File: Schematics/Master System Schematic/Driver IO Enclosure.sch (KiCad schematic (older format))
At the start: 0 parts

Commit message: New Relay Module Symbol/ Some Parts Added to Driver IO Container
(Note: Make sure to check that I didn't make some catastrophically horrible changes to everything by accident)
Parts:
- added A? (x2): Arduino_UNO_rev3, symbol NER:Arduino_UNO_rev3
- added K? (x2): G5Q-1, Relay_THT:Relay_SPDT_SANYOU_SRD_Series_Form_C, symbol Relay:G5Q-1
- added U?: CAN_Bus_Module, symbol NER:CAN_Bus_Module
- added U?: KY-019, symbol NER:KY-019
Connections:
- new net: A?.~ (~~D9), U?.~ (Serial_Clock)
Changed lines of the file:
@@
 EESchema Schematic File Version 4
-LIBS:Master System Schematic-cache
 EELAYER 30 0
 EELAYER END
@@
 Comment4 ""
 $EndDescr
+$Comp
+L Relay:G5Q-1 K?
+U 1 1 5F841D56
+P 2250 2800
+F 0 "K?" H 2680 2846 50  0000 L CNN
+F 1 "G5Q-1" H 2680 2755 50  0000 L CNN
+F 2 "Relay_THT:Relay_SPDT_SANYOU_SRD_Series_Form_C" H 2700 2750 50  0001 L CNN
+F 3 "https://www.omron.com/ecb/products/pdf/en-g5q.pdf" H 2250 2800 50  0001 L CNN
+	1    2250 2800
+	1    0    0    -1
+$EndComp
+$Comp
+L Relay:G5Q-1 K?
+U 1 1 5F84603E
+P 8500 1500
+F 0 "K?" H 8930 1546 50  0000 L CNN
+F 1 "G5Q-1" H 8930 1455 50  0000 L CNN
+F 2 "Relay_THT:Relay_SPDT_SANYOU_SRD_Series_Form_C" H 8950 1450 50  0001 L CNN
+F 3 "https://www.omron.com/ecb/products/pdf/en-g5q.pdf" H 8500 1500 50  0001 L CNN
+	1    8500 1500
+	-1   0    0    1
+$EndComp
+$Comp
+L NER:Arduino_UNO_rev3 A?
+U 1 1 5F8467E9
+P 2250 4000
+F 0 "A?" H 2250 4115 50  0000 C CNN
+F 1 "Arduino_UNO_rev3" H 2250 4024 50  0000 C CNN
+F 2 "" H 2250 4150 50  0001 C CNN
+F 3 "" H 2250 4150 50  0001 C CNN
+	1    2250 4000
+	1    0    0    -1
+$EndComp
+$Comp
+L NER:CAN_Bus_Module U?
+U 1 1 5F847676
+P 8650 2250
+F 0 "U?" H 8675 2365 50  0000 C CNN
+F 1 "CAN_Bus_Module" H 8675 2274 50  0000 C CNN
+F 2 "" H 8650 2250 50  0001 C CNN
+F 3 "" H 8650 2250 50  0001 C CNN
+	1    8650 2250
+	1    0    0    -1
+$EndComp
+$Comp
+L NER:Arduino_UNO_rev3 A?
+U 1 1 5F848DBE
+P 6800 2000
+F 0 "A?" H 6800 2115 50  0000 C CNN
+F 1 "Arduino_UNO_rev3" H 6800 2024 50  0000 C CNN
+F 2 "" H 6800 2150 50  0001 C CNN
+F 3 "" H 6800 2150 50  0001 C CNN
+	1    6800 2000
+	1    0    0    -1
+$EndComp
+Wire Wire Line
+	7400 2650 7800 2650
+Wire Wire Line
+	7800 2650 7800 2900
+Wire Wire Line
+	7800 2900 8100 2900
+$Comp
+L NER:KY-019 U?
+U 1 1 5F94DA0F
+P 3800 4300
+F 0 "U?" V 3375 4275 50  0000 C CNN
+F 1 "KY-019" V 3466 4275 50  0000 C CNN
+F 2 "" H 3750 4000 50  0001 C CNN
+F 3 "" H 3750 4000 50  0001 C CNN
+	1    3800 4300
+	0    1    1    0
+$EndComp
 $EndSCHEMATC

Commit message: Added Annotations
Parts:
- removed K? (x2): G5Q-1, Relay_THT:Relay_SPDT_SANYOU_SRD_Series_Form_C, symbol Relay:G5Q-1
- added U12: KY-019, symbol NER:KY-019
- gave numbers to parts that had none: 4
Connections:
- net at U11.~ (Serial_Clock): now also A3.~ (~~D9)
- net at A3.~ (~~D9): no longer U11.~ (Serial_Clock)
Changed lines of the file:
@@
 $EndDescr
 $Comp
-L Relay:G5Q-1 K?
-U 1 1 5F841D56
-P 2250 2800
-F 0 "K?" H 2680 2846 50  0000 L CNN
-F 1 "G5Q-1" H 2680 2755 50  0000 L CNN
-F 2 "Relay_THT:Relay_SPDT_SANYOU_SRD_Series_Form_C" H 2700 2750 50  0001 L CNN
-F 3 "https://www.omron.com/ecb/products/pdf/en-g5q.pdf" H 2250 2800 50  0001 L CNN
-	1    2250 2800
-	1    0    0    -1
-$EndComp
-$Comp
-L Relay:G5Q-1 K?
-U 1 1 5F84603E
-P 8500 1500
-F 0 "K?" H 8930 1546 50  0000 L CNN
-F 1 "G5Q-1" H 8930 1455 50  0000 L CNN
-F 2 "Relay_THT:Relay_SPDT_SANYOU_SRD_Series_Form_C" H 8950 1450 50  0001 L CNN
-F 3 "https://www.omron.com/ecb/products/pdf/en-g5q.pdf" H 8500 1500 50  0001 L CNN
-	1    8500 1500
-	-1   0    0    1
-$EndComp
-$Comp
-L NER:Arduino_UNO_rev3 A?
+L NER:Arduino_UNO_rev3 A2
 U 1 1 5F8467E9
 P 2250 4000
-F 0 "A?" H 2250 4115 50  0000 C CNN
+F 0 "A2" H 2250 4115 50  0000 C CNN
 F 1 "Arduino_UNO_rev3" H 2250 4024 50  0000 C CNN
 F 2 "" H 2250 4150 50  0001 C CNN
@@
 $EndComp
 $Comp
-L NER:CAN_Bus_Module U?
+L NER:CAN_Bus_Module U11
 U 1 1 5F847676
 P 8650 2250
-F 0 "U?" H 8675 2365 50  0000 C CNN
+F 0 "U11" H 8675 2365 50  0000 C CNN
 F 1 "CAN_Bus_Module" H 8675 2274 50  0000 C CNN
 F 2 "" H 8650 2250 50  0001 C CNN
@@
 $EndComp
 $Comp
-L NER:Arduino_UNO_rev3 A?
+L NER:Arduino_UNO_rev3 A3
 U 1 1 5F848DBE
 P 6800 2000
-F 0 "A?" H 6800 2115 50  0000 C CNN
+F 0 "A3" H 6800 2115 50  0000 C CNN
 F 1 "Arduino_UNO_rev3" H 6800 2024 50  0000 C CNN
 F 2 "" H 6800 2150 50  0001 C CNN
@@
 	7800 2900 8100 2900
 $Comp
-L NER:KY-019 U?
+L NER:KY-019 U10
 U 1 1 5F94DA0F
 P 3800 4300
-F 0 "U?" V 3375 4275 50  0000 C CNN
+F 0 "U10" V 3375 4275 50  0000 C CNN
 F 1 "KY-019" V 3466 4275 50  0000 C CNN
 F 2 "" H 3750 4000 50  0001 C CNN
@@
 	0    1    1    0
 $EndComp
+$Comp
+L NER:KY-019 U12
+U 1 1 5F8416AD
+P 8700 1450
+F 0 "U12" H 8978 1471 50  0000 L CNN
+F 1 "KY-019" H 8978 1380 50  0000 L CNN
+F 2 "" H 8650 1150 50  0001 C CNN
+F 3 "" H 8650 1150 50  0001 C CNN
+	1    8700 1450
+	1    0    0    -1
+$EndComp
 $EndSCHEMATC

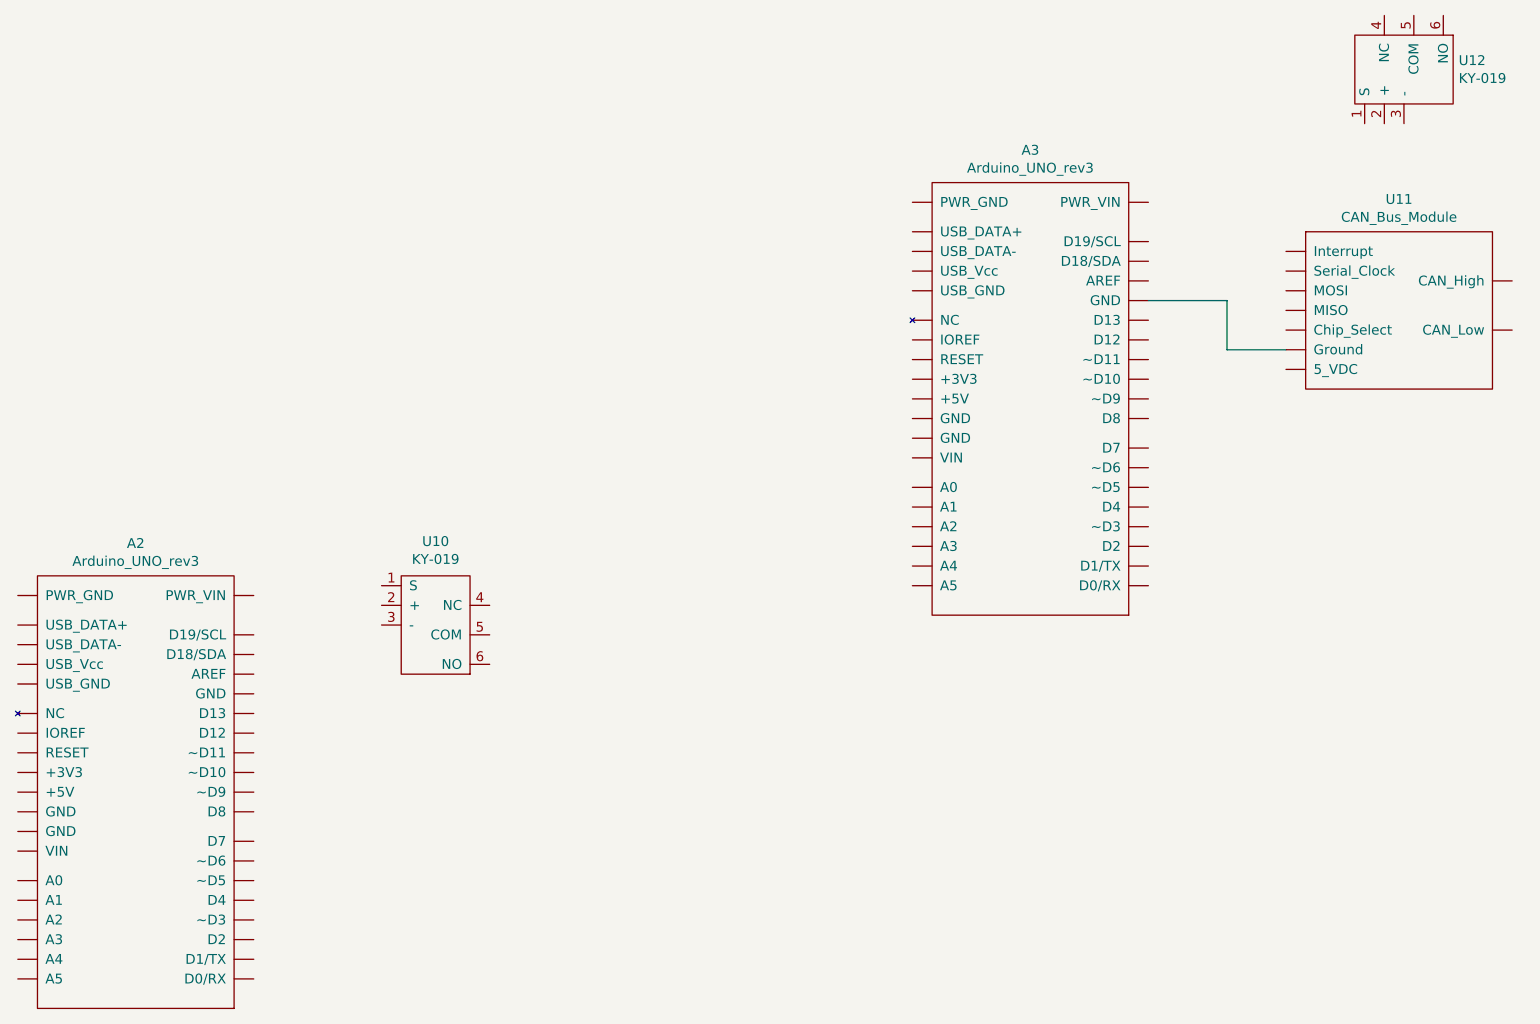
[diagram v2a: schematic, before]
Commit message: Finished IO Container, Added Brake Light
In the IO Container: made connections between Speaker, Arduino, CAN, Relay Module, and Button. Made new symbol for the Button.

In Master Schematic: added Brake Light Container.

In Brake Light Container: made connections between CAN, Relay Module, and Arduino. Still missing LED (but that will be in Master Schematic.)
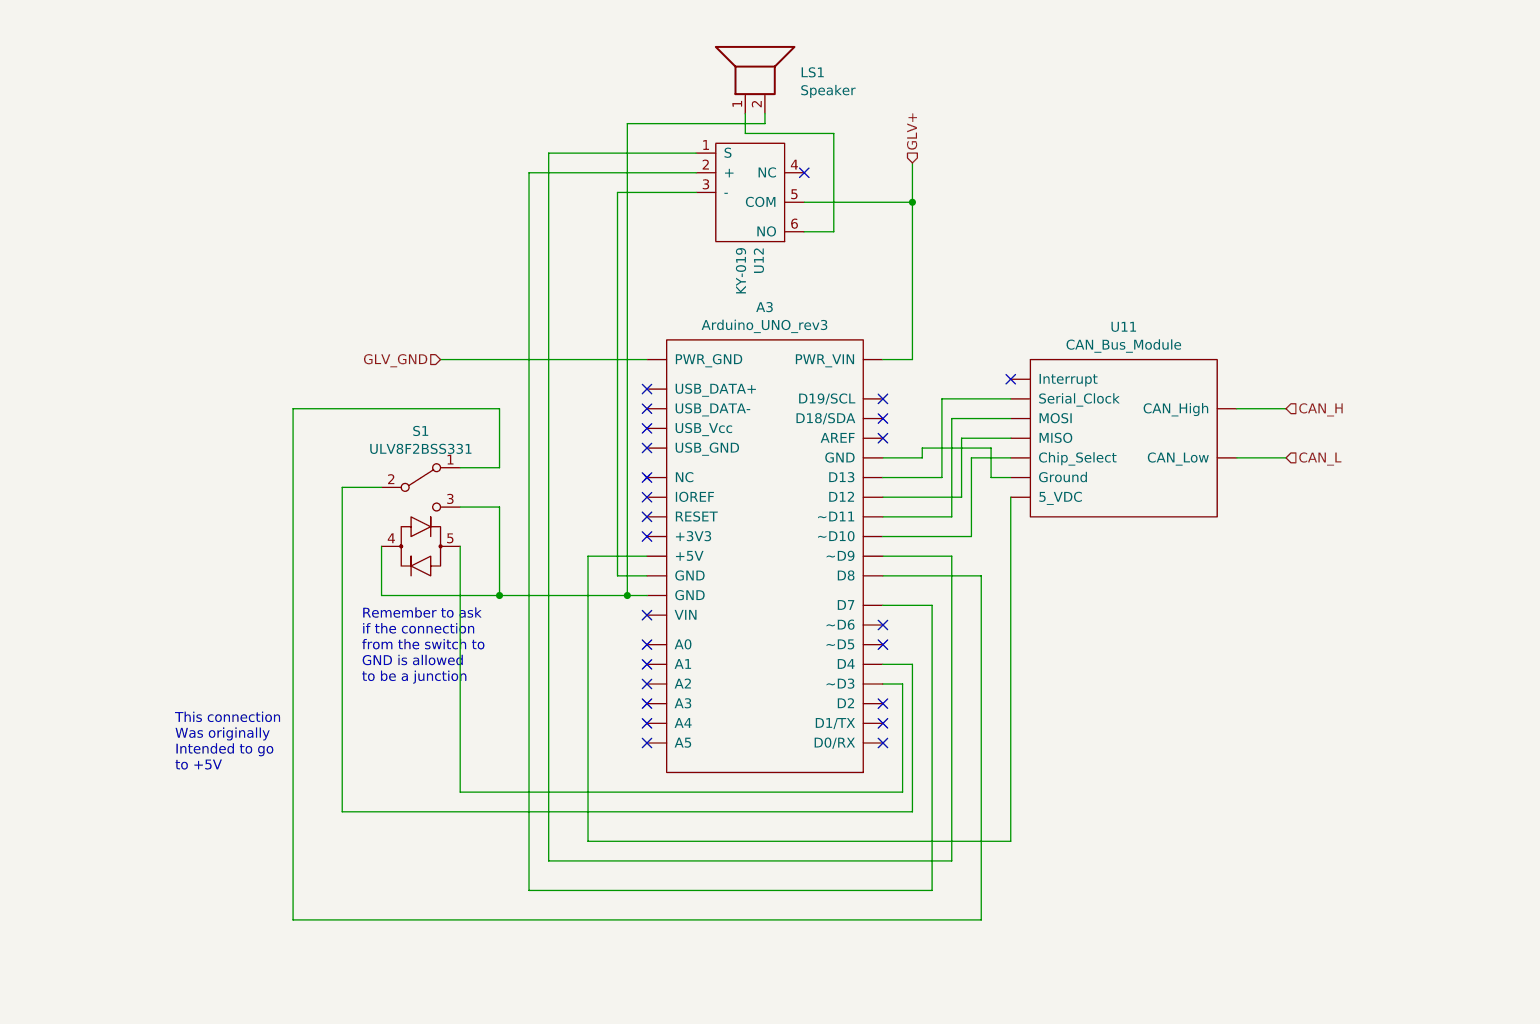
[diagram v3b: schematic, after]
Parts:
- removed A2: Arduino_UNO_rev3, symbol NER:Arduino_UNO_rev3
- removed U10: KY-019, symbol NER:KY-019
- added LS1: Speaker, symbol Device:Speaker
- added S1: ULV8F2BSS331, symbol NER:ULV8F2BSS331
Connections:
- net at U12.1 (S): now also A3.~ (~~D9)
- net at U12.2 (+): now also A3.~ (~~D9)
- net at U12.3 (-): now also A3.~ (~~D9)
- net GLV+: now reaches U12.5 (COM)
- net GLV+: now also A3.~ (~~D9)
- net at U12.6 (NO): now also LS1.1
- net CAN_L: now reaches U11.~ (Serial_Clock)
- net GLV_GND: now reaches A3.~ (~~D9)
- net GLV_GND: no longer U11.~ (Serial_Clock)
- new net: A3.~ (~~D9), U11.~ (Serial_Clock) (x6)
- new net: A3.~ (~~D9), LS1.2, S1.3 (C), S1.4 (LED(+))
- new net: A3.~ (~~D9), S1.1 (A)
- new net: A3.~ (~~D9), S1.2 (B)
- new net: A3.~ (~~D9), S1.5 (LED(-))
- new net CAN_H: U11.~ (Serial_Clock)
- no-connect marks 0 -> 25
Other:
- note added: "Remember to ask\nif the connection\nfrom the switch to\nGND is allowed\nto be a junction"
- note added: "This connection\nWas originally\nIntended to go\nto +5V"
- moved on the sheet: A3, U11, U12

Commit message: Moved Button and Speaker to Master Schematic
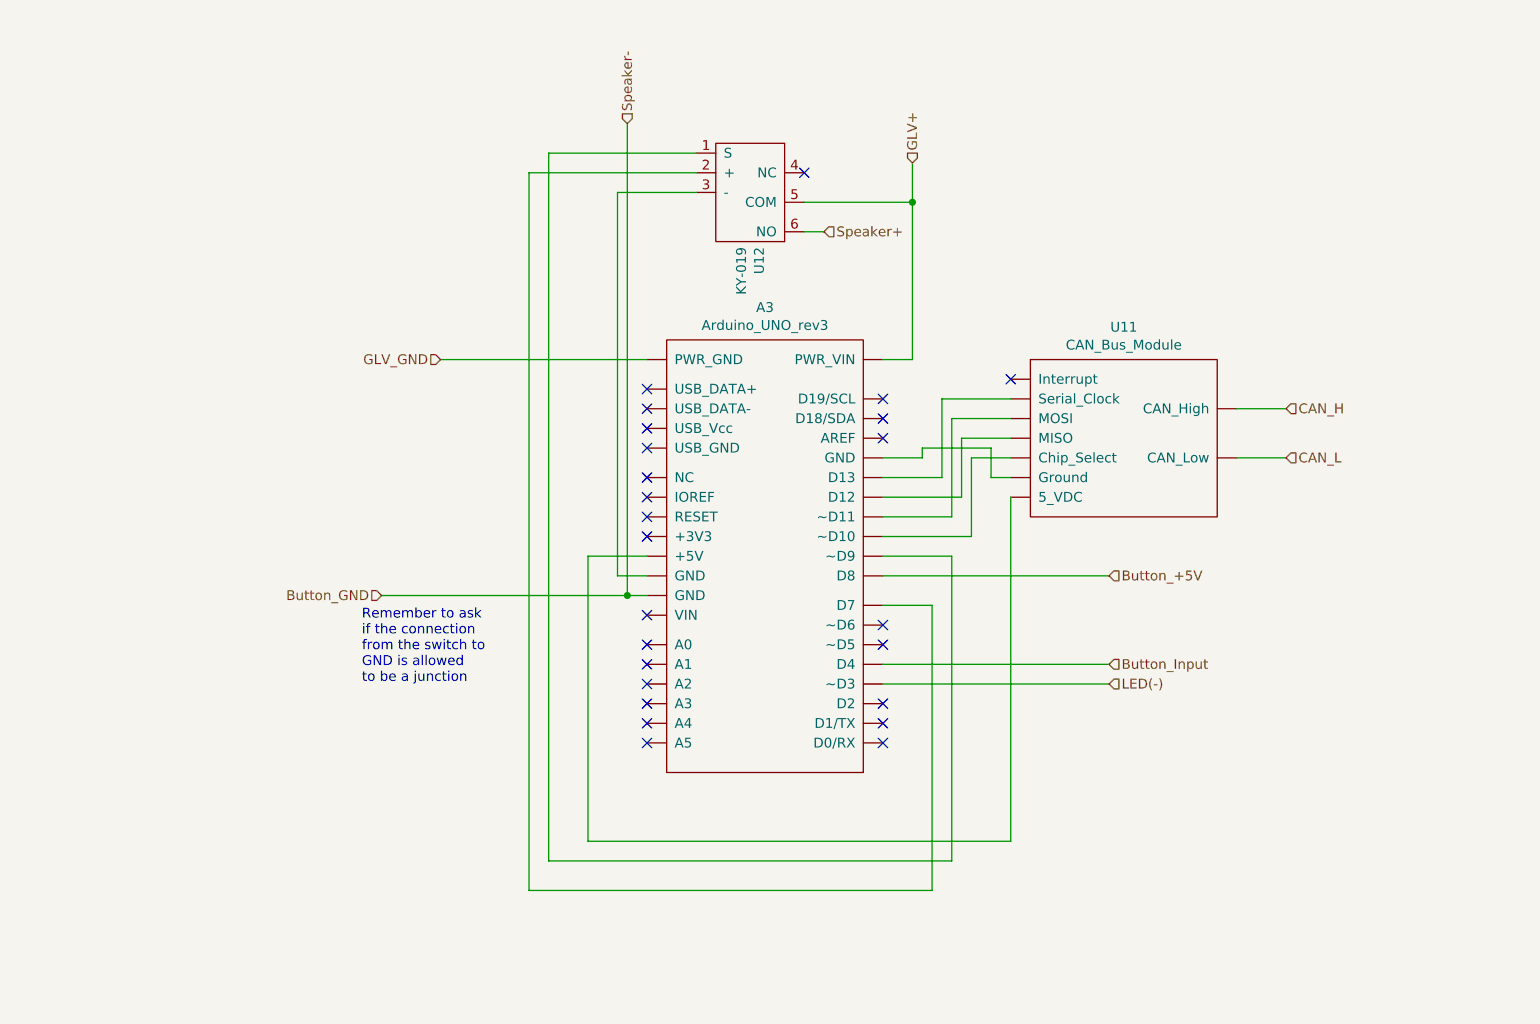
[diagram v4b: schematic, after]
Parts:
- removed LS1: Speaker, symbol Device:Speaker
- removed S1: ULV8F2BSS331, symbol NER:ULV8F2BSS331
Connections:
- net Speaker+: now reaches U12.6 (NO)
- net LED(-): now reaches A3.~ (~~D9)
- net LED(-): no longer U11.~ (Serial_Clock)
- new net: A3.~ (~~D9), U11.~ (Serial_Clock) (x6)
- new net Button_+5V: A3.~ (~~D9)
- new net Button_GND: A3.~ (~~D9)
- new net Button_Input: A3.~ (~~D9)
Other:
- note removed: "This connection\nWas originally\nIntended to go\nto +5V"
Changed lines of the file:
@@
 	0    1    1    0
-$EndComp
-$Comp
-L Device:Speaker LS1
-U 1 1 5F88B910
-P 5350 1500
-F 0 "LS1" V 5359 1220 50  0000 R CNN
-F 1 "Speaker" V 5268 1220 50  0000 R CNN
-F 2 "" H 5350 1300 50  0001 C CNN
-F 3 "~" H 5340 1450 50  0001 C CNN
-	1    5350 1500
-	0    -1   -1   0
 $EndComp
 Text HLabel 8100 3450 2    50   Input ~ 0
@@
 	4700 4050 4850 4050
 Wire Wire Line
-	5650 2300 5800 2300
-Wire Wire Line
-	5800 2300 5800 1800
-Wire Wire Line
-	5800 1800 5350 1800
-Wire Wire Line
-	5350 1800 5350 1700
-Wire Wire Line
 	4750 4150 4850 4150
-Wire Wire Line
-	5450 1700 5450 1750
-Wire Wire Line
-	5450 1750 4750 1750
 Wire Wire Line
 	4750 1750 4750 4150
@@
 NoConn ~ 4850 4250
 NoConn ~ 4850 3850
-$Comp
-L NER:ULV8F2BSS331 S1
-U 1 1 5F906A21
-P 3700 3800
-F 0 "S1" H 3700 4285 50  0000 C CNN
-F 1 "ULV8F2BSS331" H 3700 4194 50  0000 C CNN
-F 2 "" H 3700 4000 50  0001 C CNN
-F 3 "~" H 3700 4000 50  0001 C CNN
-	1    3700 3800
-	1    0    0    -1
-$EndComp
-Wire Wire Line
-	6050 4500 6200 4500
-Wire Wire Line
-	6200 4500 6200 5250
-Wire Wire Line
-	6200 5250 3300 5250
-Wire Wire Line
-	3300 5250 3300 3600
-Wire Wire Line
-	3300 3600 3500 3600
-Wire Wire Line
-	6050 4600 6150 4600
-Wire Wire Line
-	6150 4600 6150 5150
-Wire Wire Line
-	6150 5150 3900 5150
-Wire Wire Line
-	3900 5150 3900 3900
-Wire Wire Line
-	3500 3900 3500 4150
-Wire Wire Line
-	3500 4150 4100 4150
-Wire Wire Line
-	3900 3700 4100 3700
-Wire Wire Line
-	4100 3700 4100 4150
-Connection ~ 4100 4150
-Wire Wire Line
-	3900 3500 4100 3500
-Wire Wire Line
-	4100 3500 4100 3200
-Wire Wire Line
-	4100 3200 3050 3200
-Wire Wire Line
-	3050 3200 3050 5800
-Wire Wire Line
-	3050 5800 6550 5800
-Wire Wire Line
-	6550 5800 6550 4050
-Wire Wire Line
-	6550 4050 6050 4050
-Text Notes 2450 5050 0    50   ~ 0
-This connection\nWas originally\nIntended to go\nto +5V
-Wire Wire Line
-	4100 4150 4750 4150
 Connection ~ 4750 4150
 Text Notes 3400 4600 0    50   ~ 0
@@
 NoConn ~ 6050 3250
 NoConn ~ 6050 3350
+Wire Wire Line
+	6050 4600 7200 4600
+Text HLabel 7200 4600 2    50   Input ~ 0
+LED(-)
+Wire Wire Line
+	3500 4150 4750 4150
+Text HLabel 3500 4150 0    50   Input ~ 0
+Button_GND
+Text HLabel 7200 4500 2    50   Input ~ 0
+Button_Input
+Wire Wire Line
+	6050 4500 7200 4500
+Text HLabel 7200 4050 2    50   Input ~ 0
+Button_+5V
+Wire Wire Line
+	6050 4050 7200 4050
+Text HLabel 5750 2300 2    50   Input ~ 0
+Speaker+
+Text HLabel 4750 1750 1    50   Input ~ 0
+Speaker-
+Wire Wire Line
+	5650 2300 5750 2300
 $EndSCHEMATC
